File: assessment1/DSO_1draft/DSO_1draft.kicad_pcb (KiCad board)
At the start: 2 copper layers, 118 parts, among them J1 Conn_01x05, J2 Conn_Coaxial, J3 Conn_Coaxial, J4 Conn_Coaxial, J5 Conn_Coaxial, J7 USB_A_Stacked, J8 Conn_01x20, J9 Conn_01x20, SW1 SW_SPDT, U1 ADG708BRUZ, U2 ADG708BRUZ, U3 STM32G431C6Tx

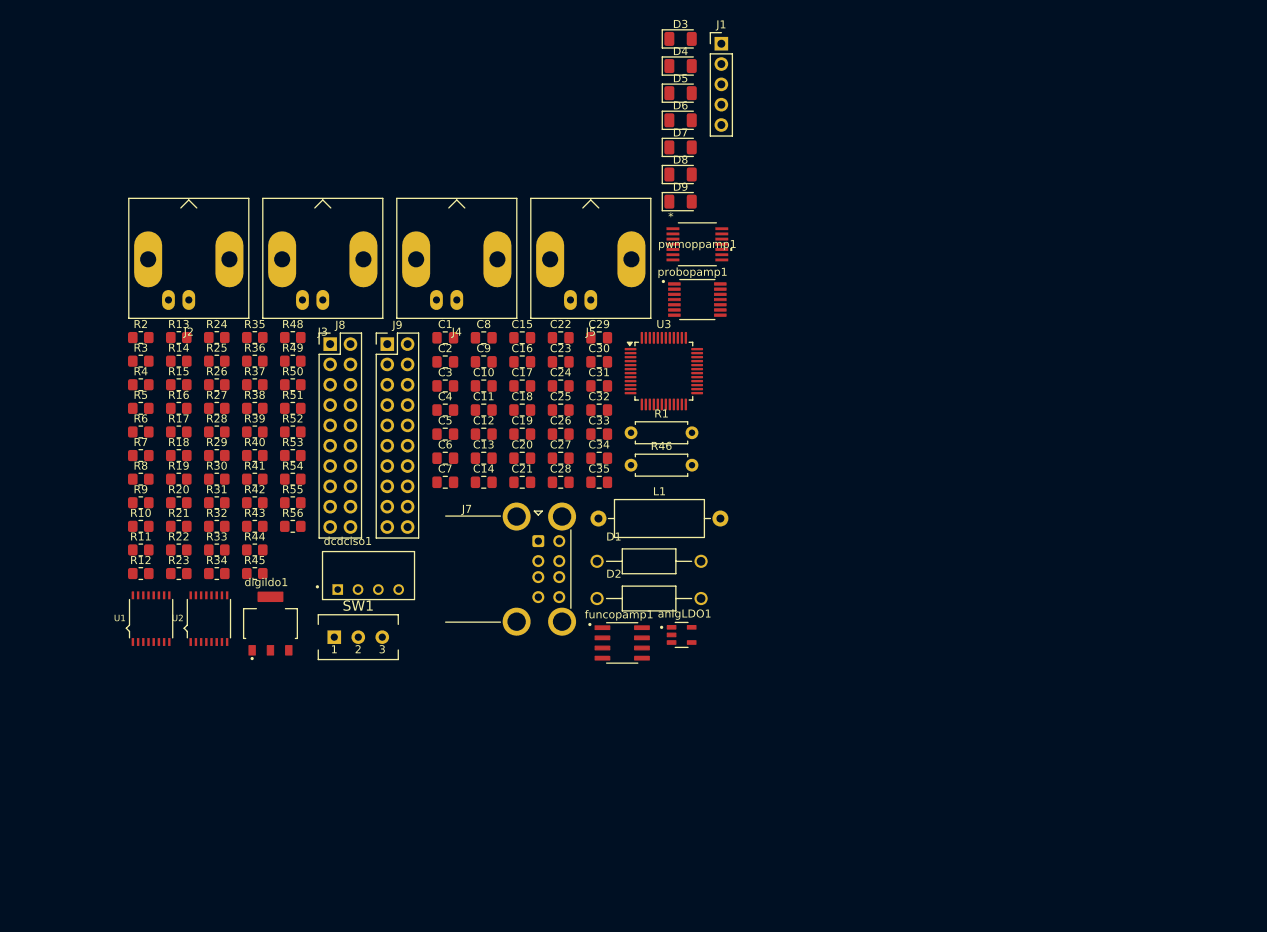
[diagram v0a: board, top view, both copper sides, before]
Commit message: updated layout
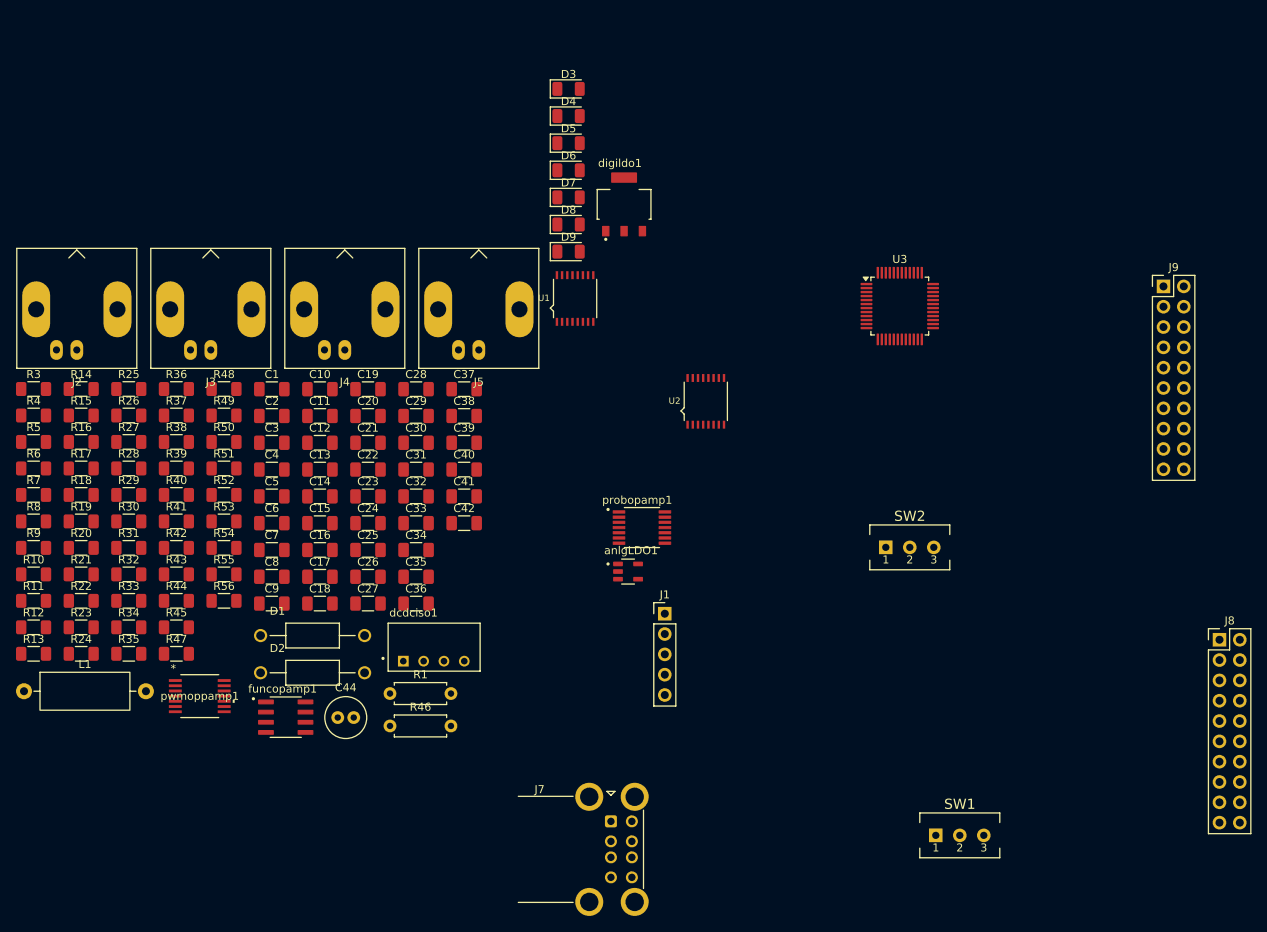
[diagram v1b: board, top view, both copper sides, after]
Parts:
- removed R2: 71.5k, Resistor_SMD:R_0805_2012Metric_Pad1.20x1.40mm_HandSolder
- added C36: 1n, Capacitor_SMD:C_1206_3216Metric_Pad1.33x1.80mm_HandSolder, F.Cu at (105.8, 113.8)
- added C37: 1n, Capacitor_SMD:C_1206_3216Metric_Pad1.33x1.80mm_HandSolder, F.Cu at (111.8, 87.0)
- added C38: 1n, Capacitor_SMD:C_1206_3216Metric_Pad1.33x1.80mm_HandSolder, F.Cu at (111.8, 90.3)
- added C39: 1n, Capacitor_SMD:C_1206_3216Metric_Pad1.33x1.80mm_HandSolder, F.Cu at (111.8, 93.7)
- added C40: 100n, Capacitor_SMD:C_1206_3216Metric_Pad1.33x1.80mm_HandSolder, F.Cu at (111.8, 97.0)
- added C41: 100n, Capacitor_SMD:C_1206_3216Metric_Pad1.33x1.80mm_HandSolder, F.Cu at (111.8, 100.4)
- added C42: 100n, Capacitor_SMD:C_1206_3216Metric_Pad1.33x1.80mm_HandSolder, F.Cu at (111.8, 103.7)
- added C44: 47u, Capacitor_THT:C_Radial_D5.0mm_H11.0mm_P2.00mm, F.Cu at (96.0, 128.0)
- added R47: 10k, Resistor_SMD:R_1206_3216Metric_Pad1.30x1.75mm_HandSolder, F.Cu at (75.8, 120.1)
- added SW2: SW_SPDT, Slide_switch:SS-12F17_1P2T, F.Cu at (167.5, 106.8)
- C1, C10, C12, C15, C18, C2, C3, C31, C32, C33, C34, C35, C4, C5, C6, C7: footprint Capacitor_SMD:C_0805_2012Metric_Pad1.18x1.45mm_HandSolder -> Capacitor_SMD:C_1206_3216Metric_Pad1.33x1.80mm_HandSolder
- C11, C14, C17, C8: value 47n -> 1n; footprint Capacitor_SMD:C_0805_2012Metric_Pad1.18x1.45mm_HandSolder -> Capacitor_SMD:C_1206_3216Metric_Pad1.33x1.80mm_HandSolder
- C13, C16, C19, C9: value 5.6n -> 1n; footprint Capacitor_SMD:C_0805_2012Metric_Pad1.18x1.45mm_HandSolder -> Capacitor_SMD:C_1206_3216Metric_Pad1.33x1.80mm_HandSolder
- C20, C22: value 2.2p -> 10p; footprint Capacitor_SMD:C_0805_2012Metric_Pad1.18x1.45mm_HandSolder -> Capacitor_SMD:C_1206_3216Metric_Pad1.33x1.80mm_HandSolder
- C21: value 300n -> 100n; footprint Capacitor_SMD:C_0805_2012Metric_Pad1.18x1.45mm_HandSolder -> Capacitor_SMD:C_1206_3216Metric_Pad1.33x1.80mm_HandSolder
- C23, C29: value 10p -> 680p; footprint Capacitor_SMD:C_0805_2012Metric_Pad1.18x1.45mm_HandSolder -> Capacitor_SMD:C_1206_3216Metric_Pad1.33x1.80mm_HandSolder
- C24, C25, C26, C27, C28, C30: value 10p -> 100p; footprint Capacitor_SMD:C_0805_2012Metric_Pad1.18x1.45mm_HandSolder -> Capacitor_SMD:C_1206_3216Metric_Pad1.33x1.80mm_HandSolder
- R10, R13, R7: value 71.5k -> 10k; footprint Resistor_SMD:R_0805_2012Metric_Pad1.20x1.40mm_HandSolder -> Resistor_SMD:R_1206_3216Metric_Pad1.30x1.75mm_HandSolder
- R11, R4, R5, R8: value 4.42k -> 10k; footprint Resistor_SMD:R_0805_2012Metric_Pad1.20x1.40mm_HandSolder -> Resistor_SMD:R_1206_3216Metric_Pad1.30x1.75mm_HandSolder
- R12, R3, R6, R9: value 56.2k -> 10k; footprint Resistor_SMD:R_0805_2012Metric_Pad1.20x1.40mm_HandSolder -> Resistor_SMD:R_1206_3216Metric_Pad1.30x1.75mm_HandSolder
- R14, R16, R17, R18, R19, R20, R22, R23, R24, R25, R27, R29, R30, R31, R32, R33, R35, R37, R38, R39, R48, R49, R50, R51, R52, R53, R54, R55, R56: footprint Resistor_SMD:R_0805_2012Metric_Pad1.20x1.40mm_HandSolder -> Resistor_SMD:R_1206_3216Metric_Pad1.30x1.75mm_HandSolder
- R15, R21, R44, R45: value R -> 1k; footprint Resistor_SMD:R_0805_2012Metric_Pad1.20x1.40mm_HandSolder -> Resistor_SMD:R_1206_3216Metric_Pad1.30x1.75mm_HandSolder
- R26, R28, R36: value 2k -> 2.2k; footprint Resistor_SMD:R_0805_2012Metric_Pad1.20x1.40mm_HandSolder -> Resistor_SMD:R_1206_3216Metric_Pad1.30x1.75mm_HandSolder
- R34: value 2K -> 2.2k; footprint Resistor_SMD:R_0805_2012Metric_Pad1.20x1.40mm_HandSolder -> Resistor_SMD:R_1206_3216Metric_Pad1.30x1.75mm_HandSolder
- R40, R41, R42, R43: value R -> 2.2k; footprint Resistor_SMD:R_0805_2012Metric_Pad1.20x1.40mm_HandSolder -> Resistor_SMD:R_1206_3216Metric_Pad1.30x1.75mm_HandSolder
- moved J8 117.1 mm to (206.2, 118.3)
- moved J9 97.3 mm to (199.2, 74.1)
- moved pwmoppamp1 84.0 mm to (78.7, 125.3)
- moved SW1 79.2 mm to (173.8, 142.8)
- moved L1 75.0 mm to (56.8, 124.7)
- moved J1 71.6 mm to (136.9, 115.0)
- moved digildo1 68.6 mm to (131.8, 63.9)
- moved U2 67.8 mm to (142.0, 88.5)
- moved U1 66.4 mm to (125.7, 75.6)
- moved R1 44.4 mm to (102.5, 125.0)
- moved R46 44.4 mm to (102.5, 129.1)
- moved R13 43.5 mm to (58.0, 120.1)
- moved funcopamp1 43.1 mm to (89.5, 128.0)
- moved D1 43.1 mm to (92.8, 117.8)
- moved D2 43.1 mm to (92.8, 122.4)
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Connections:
- C12 pad 1: Net-(C12-Pad1) -> Net-(pwmoppamp1-IN2+)
- C12 pad 2: /pwmout2 -> GND
- C13 pad 1: Net-(pwmoppamp1-IN2+) -> Net-(C13-Pad1)
- C13 pad 2: GND -> /pwmout2
- C15 pad 1: Net-(C15-Pad1) -> /pwmopout3
- C15 pad 2: /pwmout3 -> GND
- C16 pad 1: /pwmopout3 -> Net-(C16-Pad1)
- C16 pad 2: GND -> /pwmout3
- C18 pad 1: Net-(C18-Pad1) -> /pwmopout4
- C18 pad 2: /pwmout4 -> GND
- C19 pad 1: /pwmopout4 -> Net-(C19-Pad1)
- C19 pad 2: GND -> /pwmout4
- R10 pad 1: Net-(C15-Pad1) -> Net-(C16-Pad1)
- R12 pad 2: Net-(C18-Pad1) -> Net-(C19-Pad1)
- R13 pad 1: Net-(C18-Pad1) -> Net-(C19-Pad1)
- R6 pad 2: Net-(C12-Pad1) -> Net-(C13-Pad1)
- R7 pad 1: Net-(C12-Pad1) -> Net-(C13-Pad1)
- R9 pad 2: Net-(C15-Pad1) -> Net-(C16-Pad1)
- U1 pad 13: /5v -> /SelSupp
- U2 pad 13: /5v -> /SelSupp

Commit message: added switch for usb_stack
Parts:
- added SW3: SW_SPDT, Slide_switch:SS-12F17_1P2T, F.Cu at (123.4, 98.9)
- added SW4: SW_SPDT, Slide_switch:SS-12F17_1P2T, F.Cu at (123.4, 106.8)
- added SW5: SW_SPDT, Slide_switch:SS-12F17_1P2T, F.Cu at (123.4, 114.6)
- moved J8 83.3 mm to (131.5, 81.6)
- moved SW1 78.0 mm to (123.4, 83.2)
- moved R1 72.7 mm to (132.0, 58.5)
- moved R46 72.7 mm to (132.0, 62.6)
- moved J1 71.1 mm to (132.7, 44.0)
- moved D1 64.0 mm to (132.8, 67.8)
- moved D2 64.0 mm to (132.8, 72.5)
- moved J9 61.1 mm to (138.6, 81.6)
- moved anlgLDO1 54.7 mm to (79.8, 125.2)
- moved U3 54.2 mm to (134.8, 120.7)
- moved SW2 46.8 mm to (123.4, 91.1)
- moved dcdciso1 43.7 mm to (64.8, 125.5)
- moved J7 38.5 mm to (101.5, 115.3)
- moved U1 36.0 mm to (132.8, 110.9)
- moved funcopamp1 24.2 mm to (112.0, 119.2)
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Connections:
- J7 pad 2: /D- -> Net-(J7-D1-)
- J7 pad 3: /D+ -> Net-(J7-D1+)
- J7 pad 5: Net-(J7-VBUS1) -> Net-(J7-VBUS2)
- J7 pad 6: /D- -> Net-(J7-D2-)
- J7 pad 7: /D+ -> Net-(J7-D2+)
- SW1 pad 2: Net-(J7-VBUS1) -> Net-(SW1-B)

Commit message: placed some components
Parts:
- moved C28 170.6 mm to (265.2, 148.5)
- moved U3 132.8 mm to (267.6, 123.5)
- moved C37 130.5 mm to (42.0, 189.4)
- moved C41 130.5 mm to (42.0, 202.8)
- moved C29 130.5 mm to (36.0, 192.8)
- moved C30 130.5 mm to (36.0, 196.1)
- moved C31 130.5 mm to (36.0, 199.4)
- moved C32 130.5 mm to (36.0, 202.8)
- moved C33 130.5 mm to (36.0, 206.2)
- moved C38 130.5 mm to (42.0, 192.8)
- moved C39 130.5 mm to (42.0, 196.1)
- moved C40 130.5 mm to (42.0, 199.4)
- moved digildo1 107.7 mm to (67.0, 126.5), turned to 90 degrees
- moved SW2 106.6 mm to (163.0, 190.0)
- moved D5 100.7 mm to (154.1, 147.4)
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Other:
- board outline added: 85.2 x 63 mm

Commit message: modified layout placement
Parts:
- moved SW2 125.5 mm to (91.0, 87.2)
- moved J1 105.0 mm to (69.4, 86.8), turned to 90 degrees
- moved D9 103.3 mm to (88.4, 81.2), turned to 90 degrees
- moved probopamp1 103.1 mm to (90.9, 97.3)
- moved D8 102.9 mm to (85.0, 81.2), turned to 90 degrees
- moved D7 102.8 mm to (81.6, 81.2), turned to 90 degrees
- moved D6 87.9 mm to (100.3, 81.2), turned to 90 degrees
- moved D5 87.4 mm to (96.9, 81.2), turned to 90 degrees
- moved D4 87.2 mm to (93.5, 81.2), turned to 90 degrees
- moved pwmoppamp1 70.7 mm to (99.1, 135.1)
- moved C6 67.9 mm to (69.8, 116.5)
- moved C7 67.7 mm to (69.8, 120.0), turned to 180 degrees
- moved J4 53.5 mm to (212.2, 23.4), turned to 180 degrees
- moved C4 52.3 mm to (75.0, 124.5)
- moved C5 52.2 mm to (75.0, 128.0)
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
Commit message: added table for local op
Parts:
- moved funcopamp1 86.9 mm to (111.3, 116.2)
- moved pwmoppamp1 16.7 mm to (103.5, 119.0)
- moved probopamp1 14.9 mm to (102.9, 88.5)
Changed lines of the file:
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@@
 	(footprint "probingopamp:SOP65P640X120-14N"
 		(layer "F.Cu")
-		(at 90.87 97.3)
+		(at 102.88 88.45)
 		(property "Reference" "probopamp1"
 			(at -0.595 -3.435 0)
@@
 	(footprint "pwmopamp:U_TSSOP_PW_TEX-M"
 		(layer "F.Cu")
-		(at 99.05435 135.050001)
+		(at 103.5 119)
 		(tags "TLV9054IPWR ")
 		(property "Reference" "pwmoppamp1"
@@
 	(footprint "FuncOPAMP:SOIC127P599X175-8N"
 		(layer "F.Cu")
-		(at 110.745 203.0325)
+		(at 111.28 116.155)
 		(property "Reference" "funcopamp1"
 			(at -0.385 -3.537 0)
